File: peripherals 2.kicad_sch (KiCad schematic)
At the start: 14 parts, among them J601 SM04B-GHS-TB(LF)(SN), U601 SN65HVD230DR

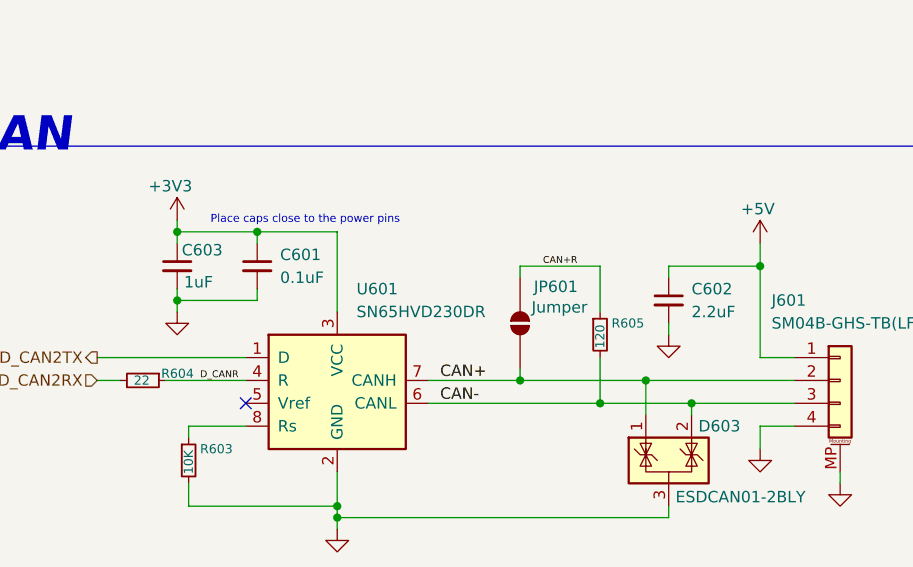
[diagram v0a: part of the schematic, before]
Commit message: refactor: change tim5 ch 1 label to ch 2
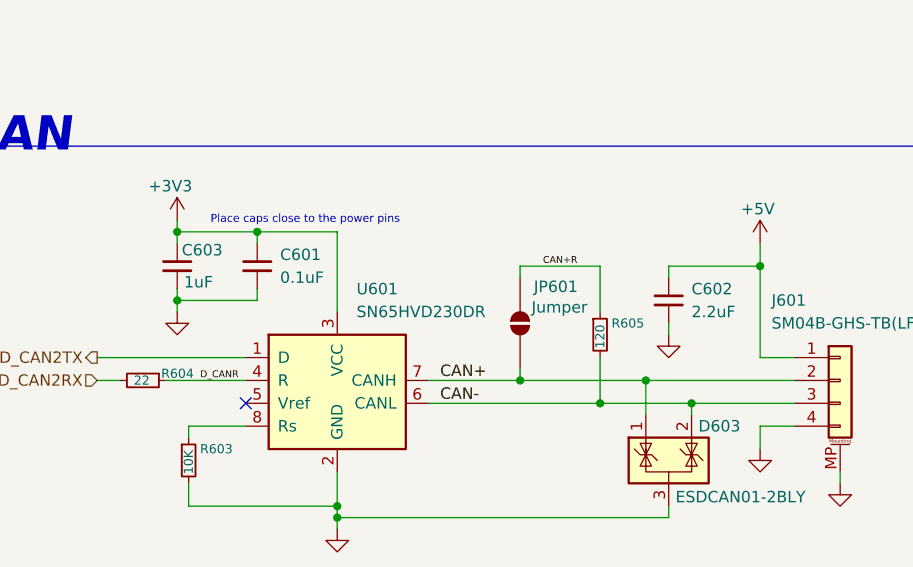
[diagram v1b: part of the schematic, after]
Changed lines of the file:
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@@
 		(fields_autoplaced yes)
 		(property "Reference" "C602"
-			(at 124.46 83.8262 0)
+			(at 124.46 83.8199 0)
 			(show_name no)
 			(do_not_autoplace no)
@@
 		)
 		(property "Value" "2.2uF"
-			(at 124.46 86.3662 0)
+			(at 124.46 86.3599 0)
 			(show_name no)
 			(do_not_autoplace no)
@@
 			)
 		)
-		(property "Description" "Ceramic Capacitor, Ceramic, 16V, 20% +Tol, 20% -Tol, X7R, 15% TC, 2.2uF, Surface Mount, 0805"
-			(at 121.92 85.09 0)
+		(property "Description" "Unpolarized capacitor, small symbol"
+			(at 121.92 95.25 0)
 			(hide yes)
 			(show_name no)
@@
 		)
 		(property "Description" "Unpolarized capacitor, small symbol"
-			(at 67.31 81.28 0)
+			(at 67.31 91.44 0)
 			(hide yes)
 			(show_name no)
@@
 		(fields_autoplaced yes)
 		(property "Reference" "C601"
-			(at 78.74 80.0162 0)
+			(at 78.74 80.0099 0)
 			(show_name no)
 			(do_not_autoplace no)
@@
 		)
 		(property "Value" "0.1uF"
-			(at 78.74 82.5562 0)
+			(at 78.74 82.5499 0)
 			(show_name no)
 			(do_not_autoplace no)
@@
 		)
 		(property "Description" "Unpolarized capacitor, small symbol"
-			(at 76.2 81.28 0)
-			(hide yes)
-			(show_name no)
+			(at 76.2 91.44 0)
+			(hide yes)
+			(show_name no)
